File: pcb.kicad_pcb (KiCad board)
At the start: 4 copper layers, 26 x 25.6 mm, 63 parts, among them J2 Conn_ARM_JTAG_SWD_10, P1 USB_C_Plug, Q1 CJE3139K, Q2 CJE3139K, Q5 2N7002, Q6 2N7002, SW1 SW_Push, U1 WE-TVS-82400102, U2 STM32F103C8T6, U6 74LVC2T45DC, U7 74LVC2T45DC, U8 74LVC2T45DC, U9 AP2112K-3.3, Y1 8MHz

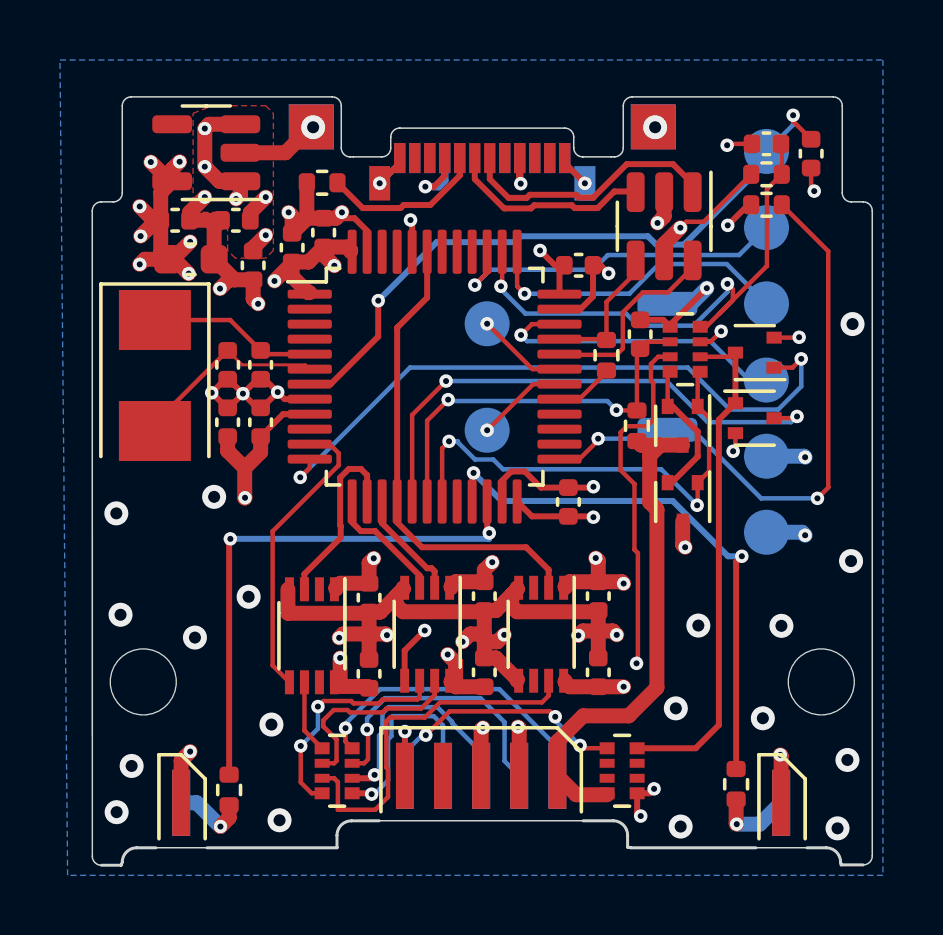
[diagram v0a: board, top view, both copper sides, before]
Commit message: update led footprint
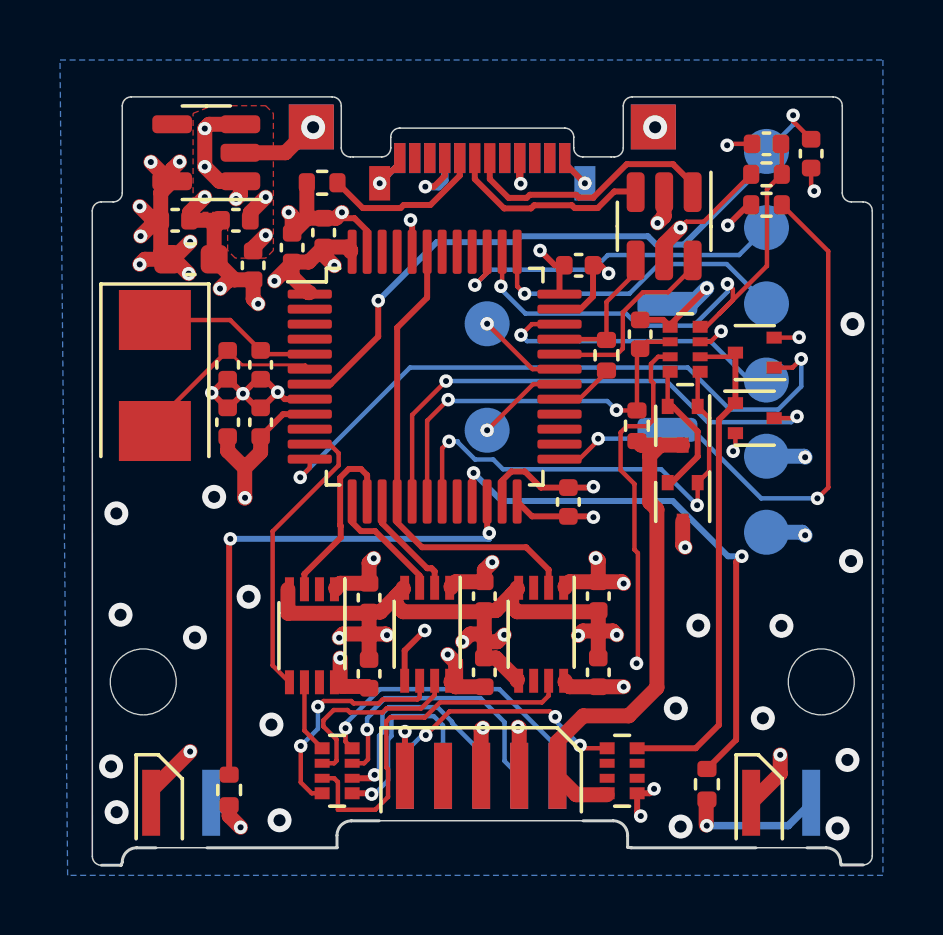
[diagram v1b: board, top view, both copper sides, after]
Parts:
- moved R9 0.97 mm to (149.3, 94.5)
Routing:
- net Net-(D2-A): track 2.60 -> 4.59 mm
- net GND: track 77.6 -> 78.4 mm
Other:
- board text added: "IDLE/RUN"
- board text removed: "IDLE"
